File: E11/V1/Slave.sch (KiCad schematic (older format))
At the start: 16 parts, among them J101 64900221122, J102 64900221122, Q101 2N7002P,215, SW101 DIP_SW_3

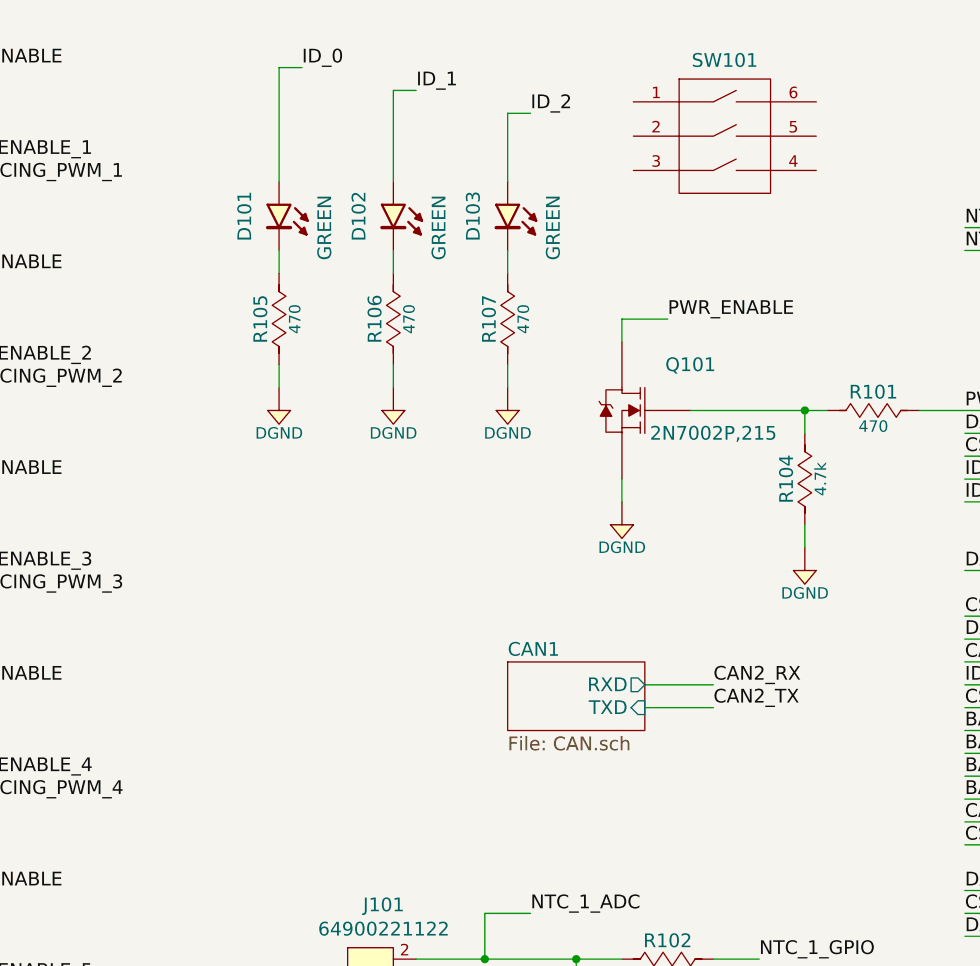
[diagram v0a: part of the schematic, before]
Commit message: update for missing resistor
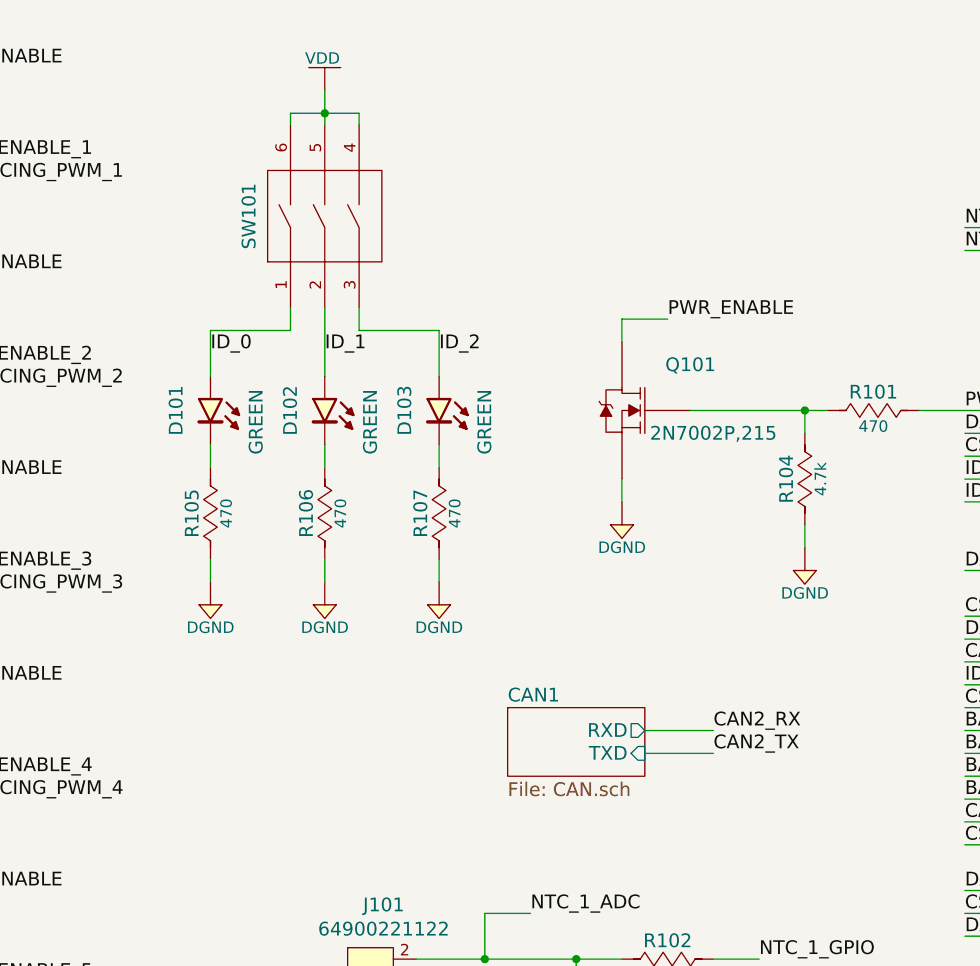
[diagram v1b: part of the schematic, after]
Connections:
- net ID_0: now also SW101.1
- net ID_1: now also SW101.2
- net ID_2: now also SW101.3
- net VDD: now also SW101.4, SW101.5, SW101.6
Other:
- moved on the sheet: D101, D102, D103, R105, R106, R107

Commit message: size reduction of modules using 0603 components
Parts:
- R105, R106, R107: value RC0805JR-07470RL -> RC0603JR-07470RL; footprint Resistors:R0805 -> Resistors:R0603; symbol Resistors:RC0805JR-07470RL -> Resistors:RC0603JR-07470RL; Description RES SMD 470 OHM 5% 1/8W 0805 -> RES SMD 470 OHM 5% 1/10W 0603; Manufacturer Part Number RC0805JR-07470RL -> RC0603JR-07470RL; Puissance (Watts) 1/8W -> 1/10W; Supplier Part Number 311-470ARCT-ND -> 311-470GRTR-ND
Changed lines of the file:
@@
 	6300 1800 6500 1800
 $Comp
-L Resistors:RC0805JR-07470RL R105
+L Resistors:RC0603JR-07470RL R105
 U 1 1 59A863F5
 P 4500 2650
 F 0 "R105" H 4500 2730 60  0000 C CNN
-F 1 "RC0805JR-07470RL" H 4500 2350 50  0001 C CNN
-F 2 "Resistors:R0805" H 4500 1750 30  0001 C CNN
-F 3 "http://www.yageo.com/documents/recent/PYu-RC_Group_51_RoHS_L_7.pdf" H 4500 1700 30  0001 C CNN
+F 1 "RC0603JR-07470RL" H 4500 2350 50  0001 C CNN
+F 2 "Resistors:R0603" H 4500 1750 30  0001 C CNN
+F 3 "https://www.yageo.com/upload/media/product/productsearch/datasheet/rchip/PYu-RC_Group_51_RoHS_L_10.pdf" H 4500 1700 30  0001 C CNN
 F 4 "Digikey" H 4500 2250 60  0001 C CNN "Supplier"
-F 5 "311-470ARCT-ND" H 4500 2150 60  0001 C CNN "Supplier Part Number"
+F 5 "311-470GRTR-ND" H 4500 2150 60  0001 C CNN "Supplier Part Number"
 F 6 "Yageo" H 4500 2050 60  0001 C CNN "Manufacturer"
-F 7 "RC0805JR-07470RL" H 4500 1950 60  0001 C CNN "Manufacturer Part Number"
-F 8 "RES SMD 470 OHM 5% 1/8W 0805" H 4500 1850 60  0001 C CNN "Description"
+F 7 "RC0603JR-07470RL" H 4500 1950 60  0001 C CNN "Manufacturer Part Number"
+F 8 "RES SMD 470 OHM 5% 1/10W 0603" H 4500 1850 60  0001 C CNN "Description"
 F 9 "470" H 4500 2580 50  0000 C CNN "Resistance (Ohms)"
 F 10 "±5%" H 4910 2570 50  0001 C CNN "Tolerance (%)"
-F 11 "1/8W" H 4500 2510 50  0001 C CNN "Puissance (Watts)"
+F 11 "1/10W" H 4500 2510 50  0001 C CNN "Puissance (Watts)"
 	1    4500 2650
 	0    -1   -1   0
 $EndComp
 $Comp
-L Resistors:RC0805JR-07470RL R106
+L Resistors:RC0603JR-07470RL R106
 U 1 1 59A87BD9
 P 5000 2650
 F 0 "R106" H 5000 2730 60  0000 C CNN
-F 1 "RC0805JR-07470RL" H 5000 2350 50  0001 C CNN
-F 2 "Resistors:R0805" H 5000 1750 30  0001 C CNN
-F 3 "http://www.yageo.com/documents/recent/PYu-RC_Group_51_RoHS_L_7.pdf" H 5000 1700 30  0001 C CNN
+F 1 "RC0603JR-07470RL" H 5000 2350 50  0001 C CNN
+F 2 "Resistors:R0603" H 5000 1750 30  0001 C CNN
+F 3 "https://www.yageo.com/upload/media/product/productsearch/datasheet/rchip/PYu-RC_Group_51_RoHS_L_10.pdf" H 5000 1700 30  0001 C CNN
 F 4 "Digikey" H 5000 2250 60  0001 C CNN "Supplier"
-F 5 "311-470ARCT-ND" H 5000 2150 60  0001 C CNN "Supplier Part Number"
+F 5 "311-470GRTR-ND" H 5000 2150 60  0001 C CNN "Supplier Part Number"
 F 6 "Yageo" H 5000 2050 60  0001 C CNN "Manufacturer"
-F 7 "RC0805JR-07470RL" H 5000 1950 60  0001 C CNN "Manufacturer Part Number"
-F 8 "RES SMD 470 OHM 5% 1/8W 0805" H 5000 1850 60  0001 C CNN "Description"
+F 7 "RC0603JR-07470RL" H 5000 1950 60  0001 C CNN "Manufacturer Part Number"
+F 8 "RES SMD 470 OHM 5% 1/10W 0603" H 5000 1850 60  0001 C CNN "Description"
 F 9 "470" H 5000 2580 50  0000 C CNN "Resistance (Ohms)"
 F 10 "±5%" H 5410 2570 50  0001 C CNN "Tolerance (%)"
-F 11 "1/8W" H 5000 2510 50  0001 C CNN "Puissance (Watts)"
+F 11 "1/10W" H 5000 2510 50  0001 C CNN "Puissance (Watts)"
 	1    5000 2650
 	0    -1   -1   0
 $EndComp
 $Comp
-L Resistors:RC0805JR-07470RL R107
+L Resistors:RC0603JR-07470RL R107
 U 1 1 59A87EBB
 P 5500 2650
 F 0 "R107" H 5500 2730 60  0000 C CNN
-F 1 "RC0805JR-07470RL" H 5500 2350 50  0001 C CNN
-F 2 "Resistors:R0805" H 5500 1750 30  0001 C CNN
-F 3 "http://www.yageo.com/documents/recent/PYu-RC_Group_51_RoHS_L_7.pdf" H 5500 1700 30  0001 C CNN
+F 1 "RC0603JR-07470RL" H 5500 2350 50  0001 C CNN
+F 2 "Resistors:R0603" H 5500 1750 30  0001 C CNN
+F 3 "https://www.yageo.com/upload/media/product/productsearch/datasheet/rchip/PYu-RC_Group_51_RoHS_L_10.pdf" H 5500 1700 30  0001 C CNN
 F 4 "Digikey" H 5500 2250 60  0001 C CNN "Supplier"
-F 5 "311-470ARCT-ND" H 5500 2150 60  0001 C CNN "Supplier Part Number"
+F 5 "311-470GRTR-ND" H 5500 2150 60  0001 C CNN "Supplier Part Number"
 F 6 "Yageo" H 5500 2050 60  0001 C CNN "Manufacturer"
-F 7 "RC0805JR-07470RL" H 5500 1950 60  0001 C CNN "Manufacturer Part Number"
-F 8 "RES SMD 470 OHM 5% 1/8W 0805" H 5500 1850 60  0001 C CNN "Description"
+F 7 "RC0603JR-07470RL" H 5500 1950 60  0001 C CNN "Manufacturer Part Number"
+F 8 "RES SMD 470 OHM 5% 1/10W 0603" H 5500 1850 60  0001 C CNN "Description"
 F 9 "470" H 5500 2580 50  0000 C CNN "Resistance (Ohms)"
 F 10 "±5%" H 5910 2570 50  0001 C CNN "Tolerance (%)"
-F 11 "1/8W" H 5500 2510 50  0001 C CNN "Puissance (Watts)"
+F 11 "1/10W" H 5500 2510 50  0001 C CNN "Puissance (Watts)"
 	1    5500 2650
 	0    -1   -1   0

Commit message: most of the parts have been migrated to new board outline
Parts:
- removed D101, D102, D103: 150080VS75000, Diodes:LED_0805_GREEN, symbol Diodes:150080VS75000
- C101, C102: footprint Capacitors:C0805 -> Capacitors:C0603; symbol Capacitors:885012107015 -> Capacitors:885012106022; Description CAP CER 1UF 25V X5R 0805 -> CAP CER 1UF 25V X5R 0603; Manufacturer Part Number 885012107015 -> 885012106022; Supplier Part Number 732-7625-1-ND -> 732-7919-2-ND
- R101: footprint Resistors:R0805 -> Resistors:R0603; symbol Resistors:RC0805JR-07470RL -> Resistors:RC0603JR-07470RL; Description RES SMD 470 OHM 5% 1/8W 0805 -> RES SMD 470 OHM 5% 1/10W 0603; Manufacturer Part Number RC0805JR-07470RL -> RC0603JR-07470RL; Puissance (Watts) 1/8W -> 1/10W; Supplier Part Number 311-470ARCT-ND -> 311-470GRTR-ND
- R102, R103: footprint Resistors:R0805 -> Resistors:R0603; symbol Resistors:RC0805JR-0733KL -> Resistors:RC0603JR-0733KL; Description RES SMD 33K OHM 5% 1/8W 0805 -> RES SMD 33K OHM 5% 1/10W 0603; Manufacturer Part Number RC0805JR-0733KL -> RC0603JR-0733KL; Puissance (Watts) 1/8W -> 1/10W; Supplier Part Number 311-33KARCT-ND -> 311-33KGRTR-ND
- R104: footprint Resistors:R0805 -> Resistors:R0603; symbol Resistors:RC0805JR-074K7L -> Resistors:RC0603JR-074K7L; Description RES SMD 4.7K OHM 5% 1/8W 0805 -> RES SMD 4.7K OHM 5% 1/10W 0603; Manufacturer Part Number RC0805JR-074K7L -> RC0603JR-074K7L; Puissance (Watts) 1/8W -> 1/10W; Supplier Part Number 311-4.7KARCT-ND -> 311-4.7KGRTR-ND
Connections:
- net ID_0: now also R105.2
- net ID_1: now also R106.2
- net ID_2: now also R107.2

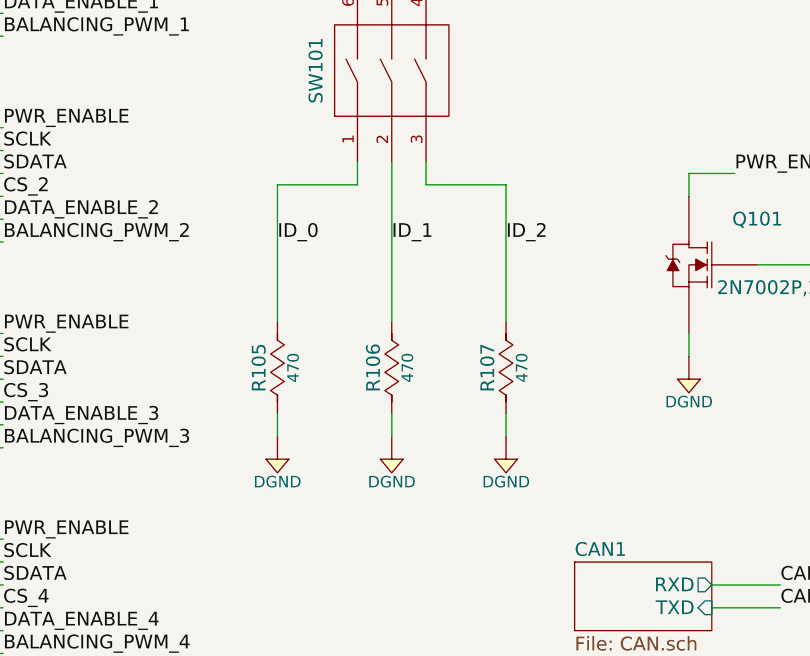
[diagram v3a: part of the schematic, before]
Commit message: initial component placement done
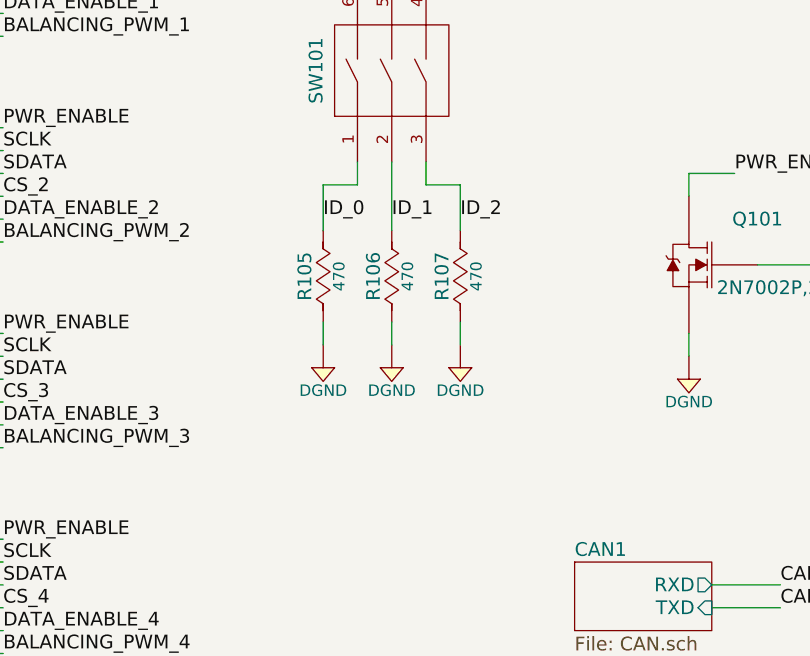
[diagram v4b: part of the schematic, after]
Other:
- moved on the sheet: R105, R106, R107
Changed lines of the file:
@@
 	6300 1800 6500 1800
-$Comp
-L Resistors:RC0603JR-07470RL R105
-U 1 1 59A863F5
-P 4500 2650
-F 0 "R105" H 4500 2730 60  0000 C CNN
-F 1 "RC0603JR-07470RL" H 4500 2350 50  0001 C CNN
-F 2 "Resistors:R0603" H 4500 1750 30  0001 C CNN
-F 3 "https://www.yageo.com/upload/media/product/productsearch/datasheet/rchip/PYu-RC_Group_51_RoHS_L_10.pdf" H 4500 1700 30  0001 C CNN
-F 4 "Digikey" H 4500 2250 60  0001 C CNN "Supplier"
-F 5 "311-470GRTR-ND" H 4500 2150 60  0001 C CNN "Supplier Part Number"
-F 6 "Yageo" H 4500 2050 60  0001 C CNN "Manufacturer"
-F 7 "RC0603JR-07470RL" H 4500 1950 60  0001 C CNN "Manufacturer Part Number"
-F 8 "RES SMD 470 OHM 5% 1/10W 0603" H 4500 1850 60  0001 C CNN "Description"
-F 9 "470" H 4500 2580 50  0000 C CNN "Resistance (Ohms)"
-F 10 "±5%" H 4910 2570 50  0001 C CNN "Tolerance (%)"
-F 11 "1/10W" H 4500 2510 50  0001 C CNN "Puissance (Watts)"
-	1    4500 2650
-	0    -1   -1   0
-$EndComp
 $Comp
 L Resistors:RC0603JR-07470RL R106
 U 1 1 59A87BD9
-P 5000 2650
-F 0 "R106" H 5000 2730 60  0000 C CNN
-F 1 "RC0603JR-07470RL" H 5000 2350 50  0001 C CNN
-F 2 "Resistors:R0603" H 5000 1750 30  0001 C CNN
-F 3 "https://www.yageo.com/upload/media/product/productsearch/datasheet/rchip/PYu-RC_Group_51_RoHS_L_10.pdf" H 5000 1700 30  0001 C CNN
-F 4 "Digikey" H 5000 2250 60  0001 C CNN "Supplier"
-F 5 "311-470GRTR-ND" H 5000 2150 60  0001 C CNN "Supplier Part Number"
-F 6 "Yageo" H 5000 2050 60  0001 C CNN "Manufacturer"
-F 7 "RC0603JR-07470RL" H 5000 1950 60  0001 C CNN "Manufacturer Part Number"
-F 8 "RES SMD 470 OHM 5% 1/10W 0603" H 5000 1850 60  0001 C CNN "Description"
-F 9 "470" H 5000 2580 50  0000 C CNN "Resistance (Ohms)"
-F 10 "±5%" H 5410 2570 50  0001 C CNN "Tolerance (%)"
-F 11 "1/10W" H 5000 2510 50  0001 C CNN "Puissance (Watts)"
-	1    5000 2650
+P 5000 2250
+F 0 "R106" H 5000 2330 60  0000 C CNN
+F 1 "RC0603JR-07470RL" H 5000 1950 50  0001 C CNN
+F 2 "Resistors:R0603" H 5000 1350 30  0001 C CNN
+F 3 "https://www.yageo.com/upload/media/product/productsearch/datasheet/rchip/PYu-RC_Group_51_RoHS_L_10.pdf" H 5000 1300 30  0001 C CNN
+F 4 "Digikey" H 5000 1850 60  0001 C CNN "Supplier"
+F 5 "311-470GRTR-ND" H 5000 1750 60  0001 C CNN "Supplier Part Number"
+F 6 "Yageo" H 5000 1650 60  0001 C CNN "Manufacturer"
+F 7 "RC0603JR-07470RL" H 5000 1550 60  0001 C CNN "Manufacturer Part Number"
+F 8 "RES SMD 470 OHM 5% 1/10W 0603" H 5000 1450 60  0001 C CNN "Description"
+F 9 "470" H 5000 2180 50  0000 C CNN "Resistance (Ohms)"
+F 10 "±5%" H 5410 2170 50  0001 C CNN "Tolerance (%)"
+F 11 "1/10W" H 5000 2110 50  0001 C CNN "Puissance (Watts)"
+	1    5000 2250
 	0    -1   -1   0
 $EndComp
@@
 L Resistors:RC0603JR-07470RL R107
 U 1 1 59A87EBB
-P 5500 2650
-F 0 "R107" H 5500 2730 60  0000 C CNN
-F 1 "RC0603JR-07470RL" H 5500 2350 50  0001 C CNN
-F 2 "Resistors:R0603" H 5500 1750 30  0001 C CNN
-F 3 "https://www.yageo.com/upload/media/product/productsearch/datasheet/rchip/PYu-RC_Group_51_RoHS_L_10.pdf" H 5500 1700 30  0001 C CNN
-F 4 "Digikey" H 5500 2250 60  0001 C CNN "Supplier"
-F 5 "311-470GRTR-ND" H 5500 2150 60  0001 C CNN "Supplier Part Number"
-F 6 "Yageo" H 5500 2050 60  0001 C CNN "Manufacturer"
-F 7 "RC0603JR-07470RL" H 5500 1950 60  0001 C CNN "Manufacturer Part Number"
-F 8 "RES SMD 470 OHM 5% 1/10W 0603" H 5500 1850 60  0001 C CNN "Description"
-F 9 "470" H 5500 2580 50  0000 C CNN "Resistance (Ohms)"
-F 10 "±5%" H 5910 2570 50  0001 C CNN "Tolerance (%)"
-F 11 "1/10W" H 5500 2510 50  0001 C CNN "Puissance (Watts)"
-	1    5500 2650
+P 5300 2250
+F 0 "R107" H 5300 2330 60  0000 C CNN
+F 1 "RC0603JR-07470RL" H 5300 1950 50  0001 C CNN
+F 2 "Resistors:R0603" H 5300 1350 30  0001 C CNN
+F 3 "https://www.yageo.com/upload/media/product/productsearch/datasheet/rchip/PYu-RC_Group_51_RoHS_L_10.pdf" H 5300 1300 30  0001 C CNN
+F 4 "Digikey" H 5300 1850 60  0001 C CNN "Supplier"
+F 5 "311-470GRTR-ND" H 5300 1750 60  0001 C CNN "Supplier Part Number"
+F 6 "Yageo" H 5300 1650 60  0001 C CNN "Manufacturer"
+F 7 "RC0603JR-07470RL" H 5300 1550 60  0001 C CNN "Manufacturer Part Number"
+F 8 "RES SMD 470 OHM 5% 1/10W 0603" H 5300 1450 60  0001 C CNN "Description"
+F 9 "470" H 5300 2180 50  0000 C CNN "Resistance (Ohms)"
+F 10 "±5%" H 5710 2170 50  0001 C CNN "Tolerance (%)"
+F 11 "1/10W" H 5300 2110 50  0001 C CNN "Puissance (Watts)"
+	1    5300 2250
 	0    -1   -1   0
 $EndComp
@@
 L Power_Port:DGND #PWR0117
 U 1 1 59A8AD26
-P 4500 3050
-F 0 "#PWR0117" H 4500 2880 50  0001 C CNN
-F 1 "DGND" H 4500 2950 50  0000 C CNN
-F 2 "" H 4500 3150 60  0000 C CNN
-F 3 "" H 4480 2960 60  0000 C CNN
-	1    4500 3050
+P 4700 2650
+F 0 "#PWR0117" H 4700 2480 50  0001 C CNN
+F 1 "DGND" H 4700 2550 50  0000 C CNN
+F 2 "" H 4700 2750 60  0000 C CNN
+F 3 "" H 4680 2560 60  0000 C CNN
+	1    4700 2650
 	1    0    0    -1
 $EndComp
@@
 L Power_Port:DGND #PWR0118
 U 1 1 59A8AFEC
-P 5000 3050
-F 0 "#PWR0118" H 5000 2880 50  0001 C CNN
-F 1 "DGND" H 5000 2950 50  0000 C CNN
-F 2 "" H 5000 3150 60  0000 C CNN
-F 3 "" H 4980 2960 60  0000 C CNN
-	1    5000 3050
+P 5000 2650
+F 0 "#PWR0118" H 5000 2480 50  0001 C CNN
+F 1 "DGND" H 5000 2550 50  0000 C CNN
+F 2 "" H 5000 2750 60  0000 C CNN
+F 3 "" H 4980 2560 60  0000 C CNN
+	1    5000 2650
 	1    0    0    -1
 $EndComp
@@
 L Power_Port:DGND #PWR0119
 U 1 1 59A8B2B2
-P 5500 3050
-F 0 "#PWR0119" H 5500 2880 50  0001 C CNN
-F 1 "DGND" H 5500 2950 50  0000 C CNN
-F 2 "" H 5500 3150 60  0000 C CNN
-F 3 "" H 5480 2960 60  0000 C CNN
-	1    5500 3050
-	1    0    0    -1
-$EndComp
-Wire Wire Line
-	5500 2850 5500 2950
-Wire Wire Line
-	5000 2850 5000 2950
-Wire Wire Line
-	4500 2850 4500 2950
+P 5300 2650
+F 0 "#PWR0119" H 5300 2480 50  0001 C CNN
+F 1 "DGND" H 5300 2550 50  0000 C CNN
+F 2 "" H 5300 2750 60  0000 C CNN
+F 3 "" H 5280 2560 60  0000 C CNN
+	1    5300 2650
+	1    0    0    -1
+$EndComp
+Wire Wire Line
+	5300 2450 5300 2550
+Wire Wire Line
+	5000 2450 5000 2550
+Wire Wire Line
+	4700 2450 4700 2550
 Text Label 7800 3400 0    60   ~ 0
 ID_0
-Text Label 4500 2100 0    60   ~ 0
+Text Label 4700 2000 0    60   ~ 0
 ID_0
-Text Label 5000 2100 0    60   ~ 0
+Text Label 5000 2000 0    60   ~ 0
 ID_1
-Text Label 5500 2100 0    60   ~ 0
+Text Label 5300 2000 0    60   ~ 0
 ID_2
 Text Label 7800 2500 0    60   ~ 0
@@
 $EndComp
 Wire Wire Line
-	5150 1850 5500 1850
-Wire Wire Line
-	4850 1850 4500 1850
-Wire Wire Line
-	5500 1850 5500 2450
-Wire Wire Line
-	4500 1850 4500 2450
-Wire Wire Line
-	5000 1750 5000 2450
+	5150 1850 5300 1850
 $Comp
 L Switches:DIP_SW_3 SW101
@@
 	0    -1   -1   0
 $EndComp
+$Comp
+L Resistors:RC0603JR-07470RL R105
+U 1 1 59A863F5
+P 4700 2250
+F 0 "R105" H 4700 2330 60  0000 C CNN
+F 1 "RC0603JR-07470RL" H 4700 1950 50  0001 C CNN
+F 2 "Resistors:R0603" H 4700 1350 30  0001 C CNN
+F 3 "https://www.yageo.com/upload/media/product/productsearch/datasheet/rchip/PYu-RC_Group_51_RoHS_L_10.pdf" H 4700 1300 30  0001 C CNN
+F 4 "Digikey" H 4700 1850 60  0001 C CNN "Supplier"
+F 5 "311-470GRTR-ND" H 4700 1750 60  0001 C CNN "Supplier Part Number"
+F 6 "Yageo" H 4700 1650 60  0001 C CNN "Manufacturer"
+F 7 "RC0603JR-07470RL" H 4700 1550 60  0001 C CNN "Manufacturer Part Number"
+F 8 "RES SMD 470 OHM 5% 1/10W 0603" H 4700 1450 60  0001 C CNN "Description"
+F 9 "470" H 4700 2180 50  0000 C CNN "Resistance (Ohms)"
+F 10 "±5%" H 5110 2170 50  0001 C CNN "Tolerance (%)"
+F 11 "1/10W" H 4700 2110 50  0001 C CNN "Puissance (Watts)"
+	1    4700 2250
+	0    -1   -1   0
+$EndComp
+Wire Wire Line
+	4700 2050 4700 1850
+Wire Wire Line
+	5300 2050 5300 1850
+Wire Wire Line
+	4700 1850 4850 1850
+Wire Wire Line
+	5000 2050 5000 1750
 $EndSCHEMATC
